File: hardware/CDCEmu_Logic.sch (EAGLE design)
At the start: 28 parts, among them J1 CAN, J2 ICSP, Q1 BC546A, U1 7805, U2 ATTINY85, U3 MCP2515, U4 1050, U5 PCF8574P, Y1 8MHz

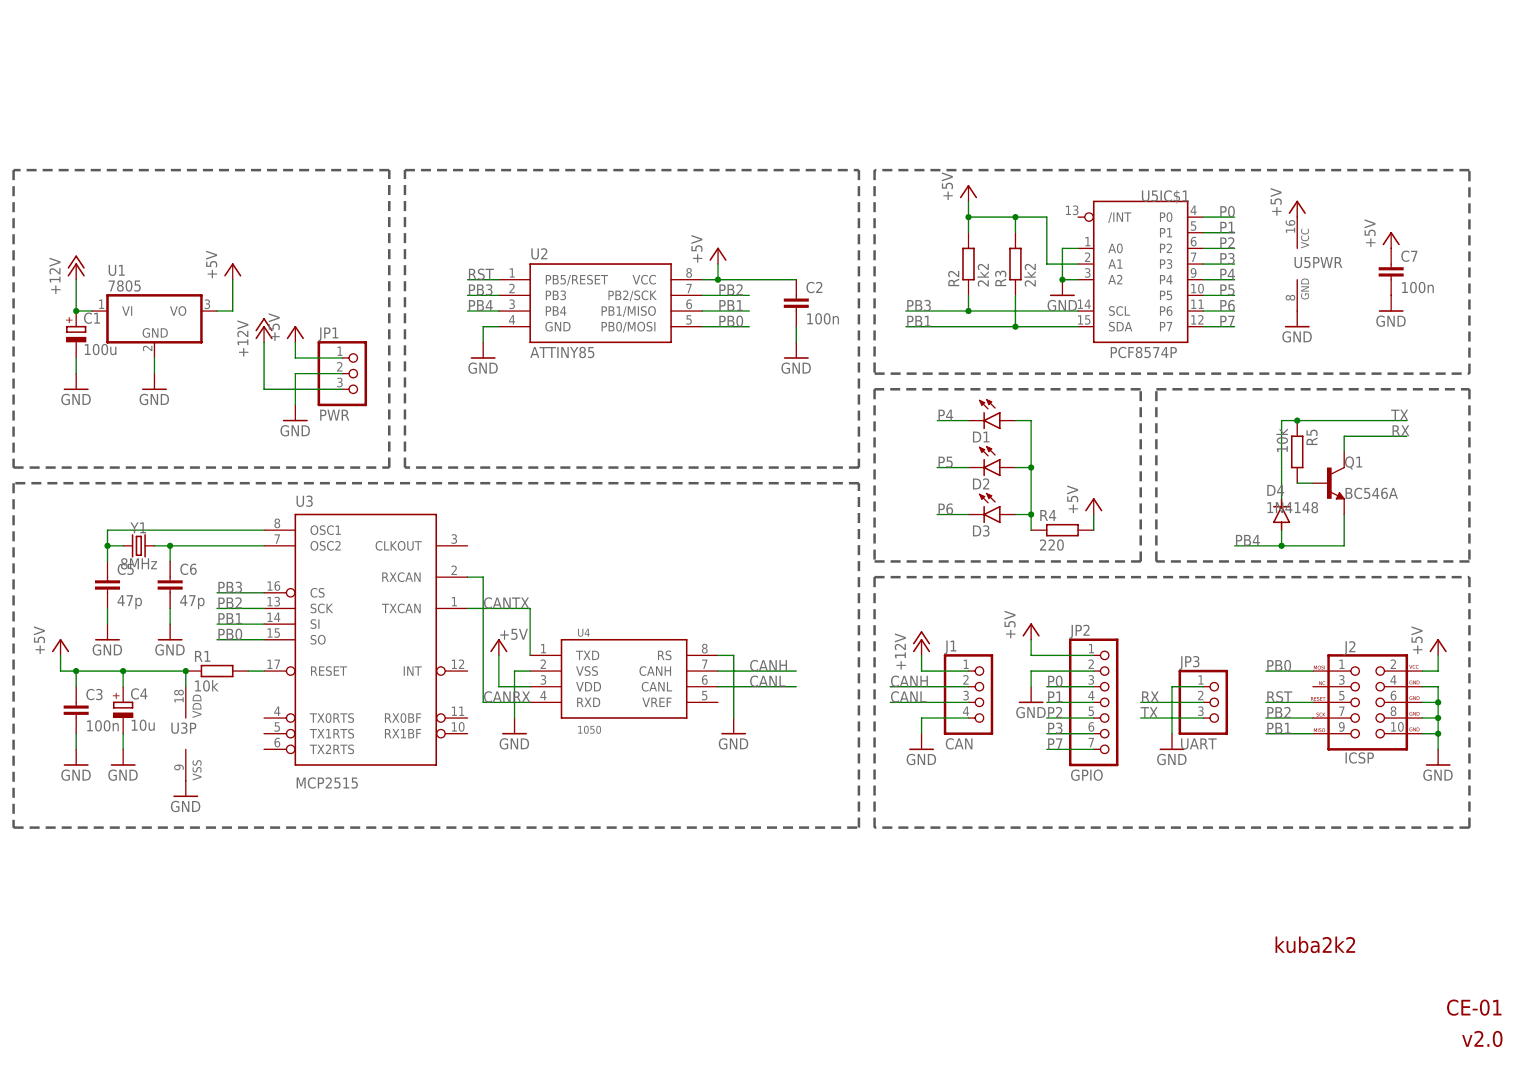
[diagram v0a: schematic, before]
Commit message: [HW] Refactor logic PCB
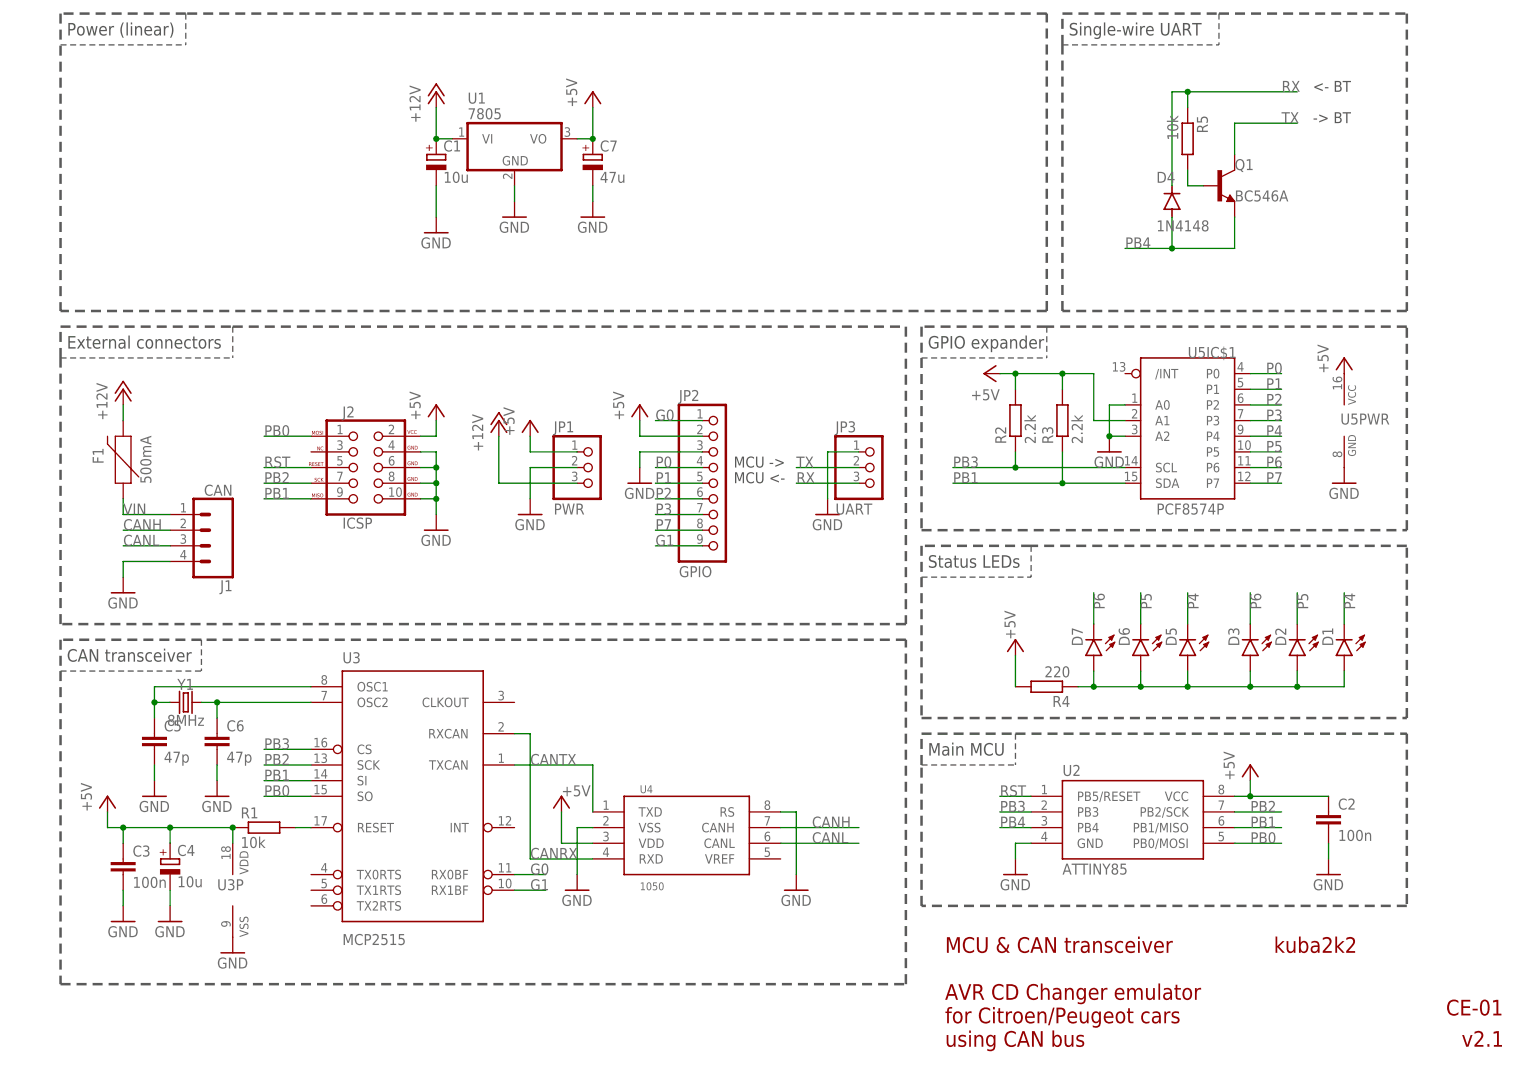
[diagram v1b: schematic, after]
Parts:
- added D5, D6, D7: (no value), led:LEDCHIP-LED0805
- added F1: 500mA, SparkFun-Fuses:PPTC_16V_2.5A
- C1: value 100u -> 10u; device rcl:CPOL-EUE2.5-6 -> custom:CPOL-EUC2512
- C4: device rcl:CPOL-EUE1.8-4 -> rcl:CPOL-EUE2.5-6
- C5, C6: device rcl:C-EU025-024X044 -> rcl:C-EUC0805
- C7: value 100n -> 47u; device rcl:C-EU050-024X044 -> custom:CPOL-EUC2512
- J1: device pinhead:PINHD-1X4 -> SparkFun-Connectors:CONN_04JST-PTH
- JP2: device pinhead:PINHD-1X7 -> pinhead:PINHD-1X9
- R1: device rcl:R-EU_0204/5 -> rcl:R-EU_R0805
- R2, R3: value 2k2 -> 2.2k; device rcl:R-EU_0204/7 -> rcl:R-EU_R0805
- U1: device linear:7805TV -> custom:78T-NOHOLE
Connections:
- new net G0: JP2.1, U3>NAME.RX0BF
- new net G1: JP2.9, U3>NAME.RX1BF
- new net VIN: F1.1, J1.1
- net +12V: now also F1.2; no longer J1.1
- net +5V: now also C7.+, JP2.2; no longer C7.1, JP2.1
- net GND: now also C7.-, JP2.3; no longer C7.2, JP2.2
- net LED_A: now also D5.A, D6.A, D7.A
- net P0: now also JP2.4; no longer JP2.3
- net P1: now also JP2.5; no longer JP2.4
- net P2: now also JP2.6; no longer JP2.5
- net P3: now also JP2.7; no longer JP2.6
- net P4: now also D5.C
- net P5: now also D6.C
- net P6: now also D7.C
- net P7: now also JP2.8; no longer JP2.7
- net RX: now also D4.C, JP3.3, R5.1; no longer JP3.2, Q1.C
- net TX: now also JP3.2, Q1.C; no longer D4.C, JP3.3, R5.1
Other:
- note added: "-> BT"
- note added: "<- BT"
- note added: "AVR CD Changer emulator for Citroen/Peugeot cars using CAN bus"
- note added: "CAN transceiver"
- note added: "External connectors"
- note added: "GPIO expander"
- note added: "MCU & CAN transceiver"
- note added: "MCU ->"
- note added: "MCU <-"
- note added: "Main MCU"
- note added: "Power (linear)"
- note added: "Single-wire UART"
- note added: "Status LEDs"
- note added: "v2.1"
- note removed: "v2.0"
- moved on the sheet: C1, C2, C3, C4, C5, C6, D1, D2, D3, D4, J2, JP1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
